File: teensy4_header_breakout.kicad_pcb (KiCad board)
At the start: 2 copper layers, 22.9 x 35.6 mm, 3 parts, among them J1 Conn_01x14, J2 Conn_01x14, U1 GND-1

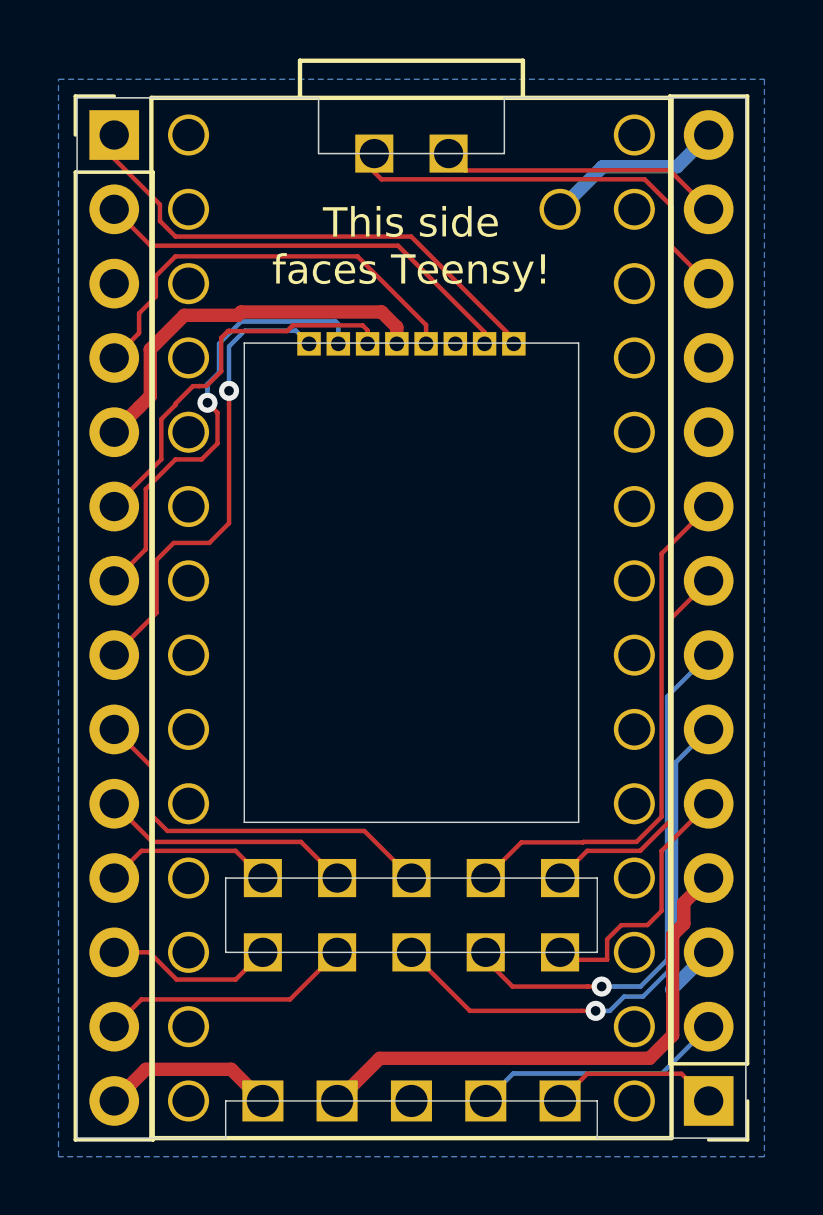
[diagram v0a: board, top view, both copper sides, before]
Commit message: add pin labels to silkscreen
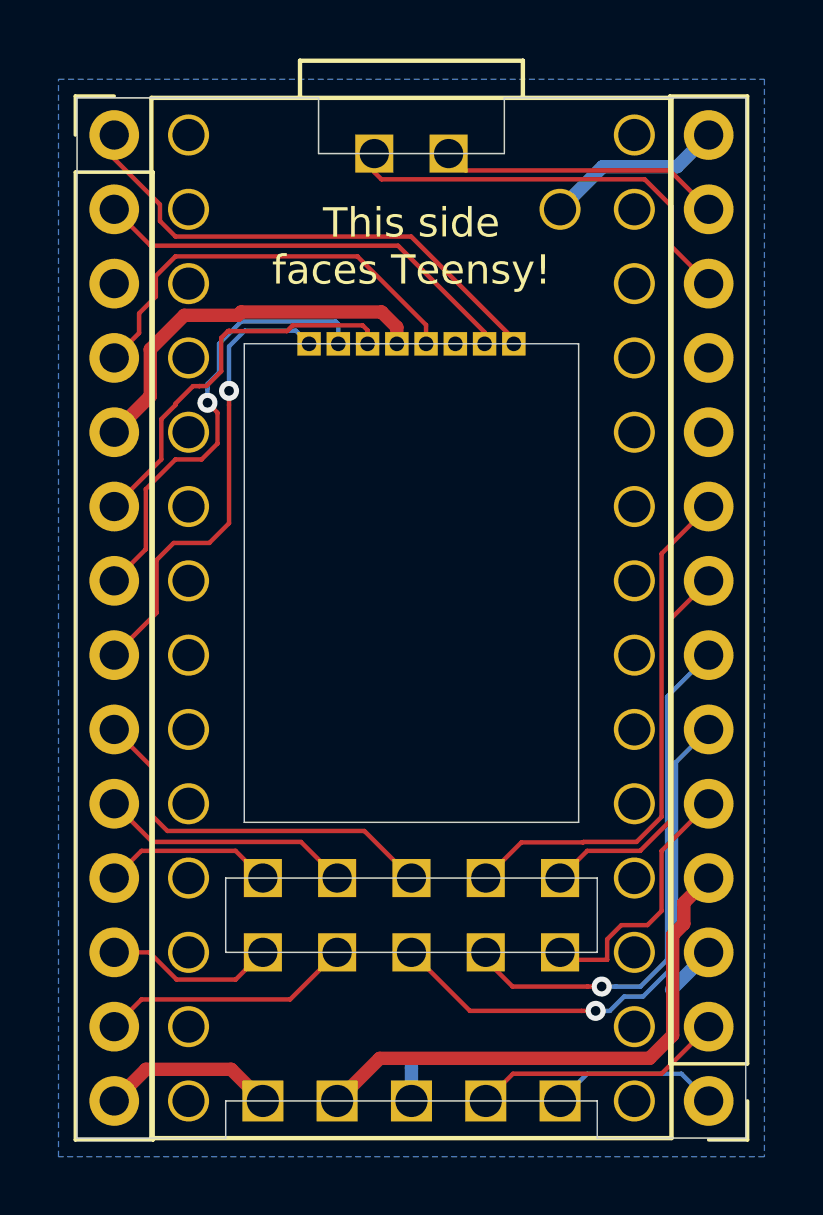
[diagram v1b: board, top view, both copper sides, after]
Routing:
- net /GND: track 1.85 -> 2.63 mm
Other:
- board text added: "24"
- board text added: "25"
- board text added: "26"
- board text added: "27"
- board text added: "28"
- board text added: "29"
- board text added: "30"
- board text added: "31"
- board text added: "32"
- board text added: "33"
- board text added: "34"
- board text added: "35"
- board text added: "36"
- board text added: "37"
- board text added: "38"
- board text added: "39"
- board text added: "3v3"
- board text added: "D+"
- board text added: "D-"
- board text added: "gnd"
- board text added: "on-off"
- board text added: "pgm"
- board text added: "vbat"
- board text added: "vusb"

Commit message: More ground plane, add todo
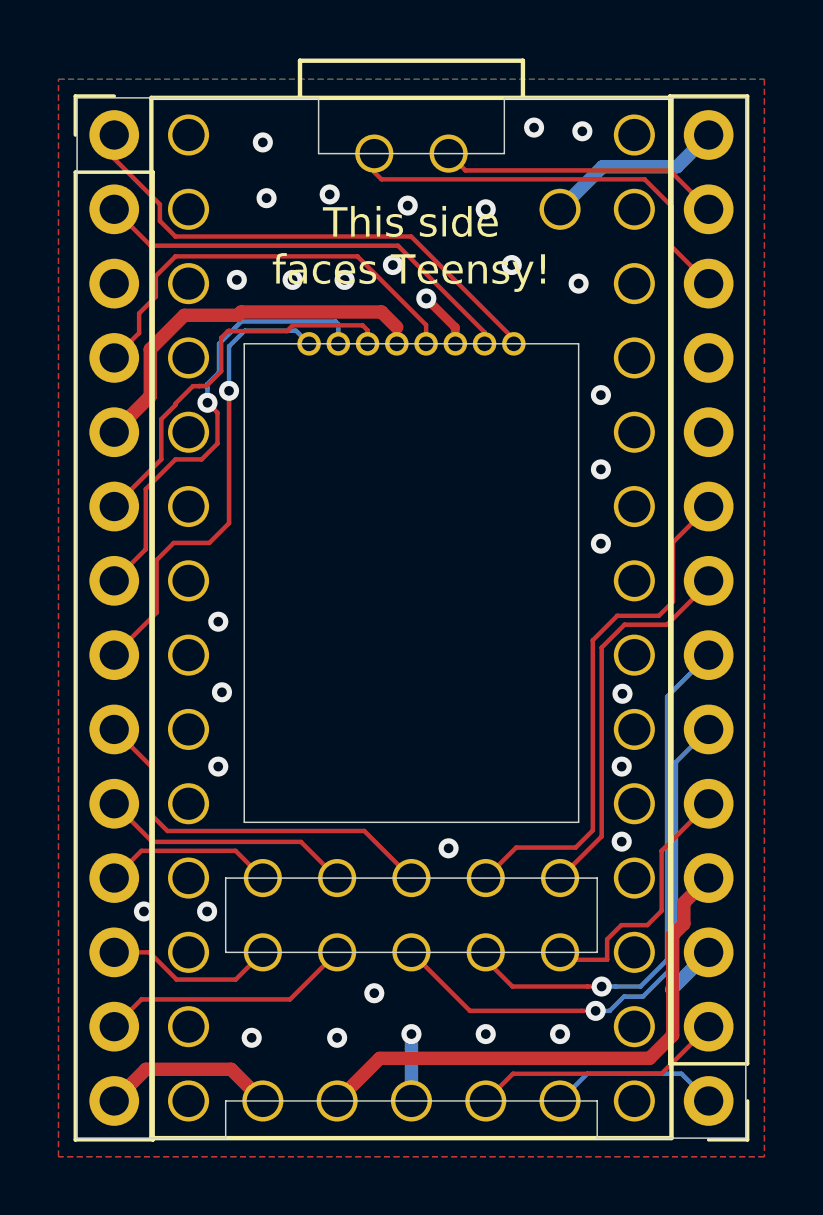
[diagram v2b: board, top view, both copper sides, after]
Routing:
- net /GND: track 2.63 -> 5.36 mm, vias 0 -> 32
- added copper zone on F.Cu, net /GND
